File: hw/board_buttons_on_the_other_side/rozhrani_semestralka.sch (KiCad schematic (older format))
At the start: 59 parts, among them P1 DISPLAY_CONN, P2 DISPLAY_VCC_CON, P3 USB_B, Q1 BC847, U1 MCP2210, U2 MIC5504-3.3, U3 Joystick, U4 LM239, U5 CD4532, U6 NPIC6C596, U7 NE555, U8 PB6149L, U9 PB6149Ldual

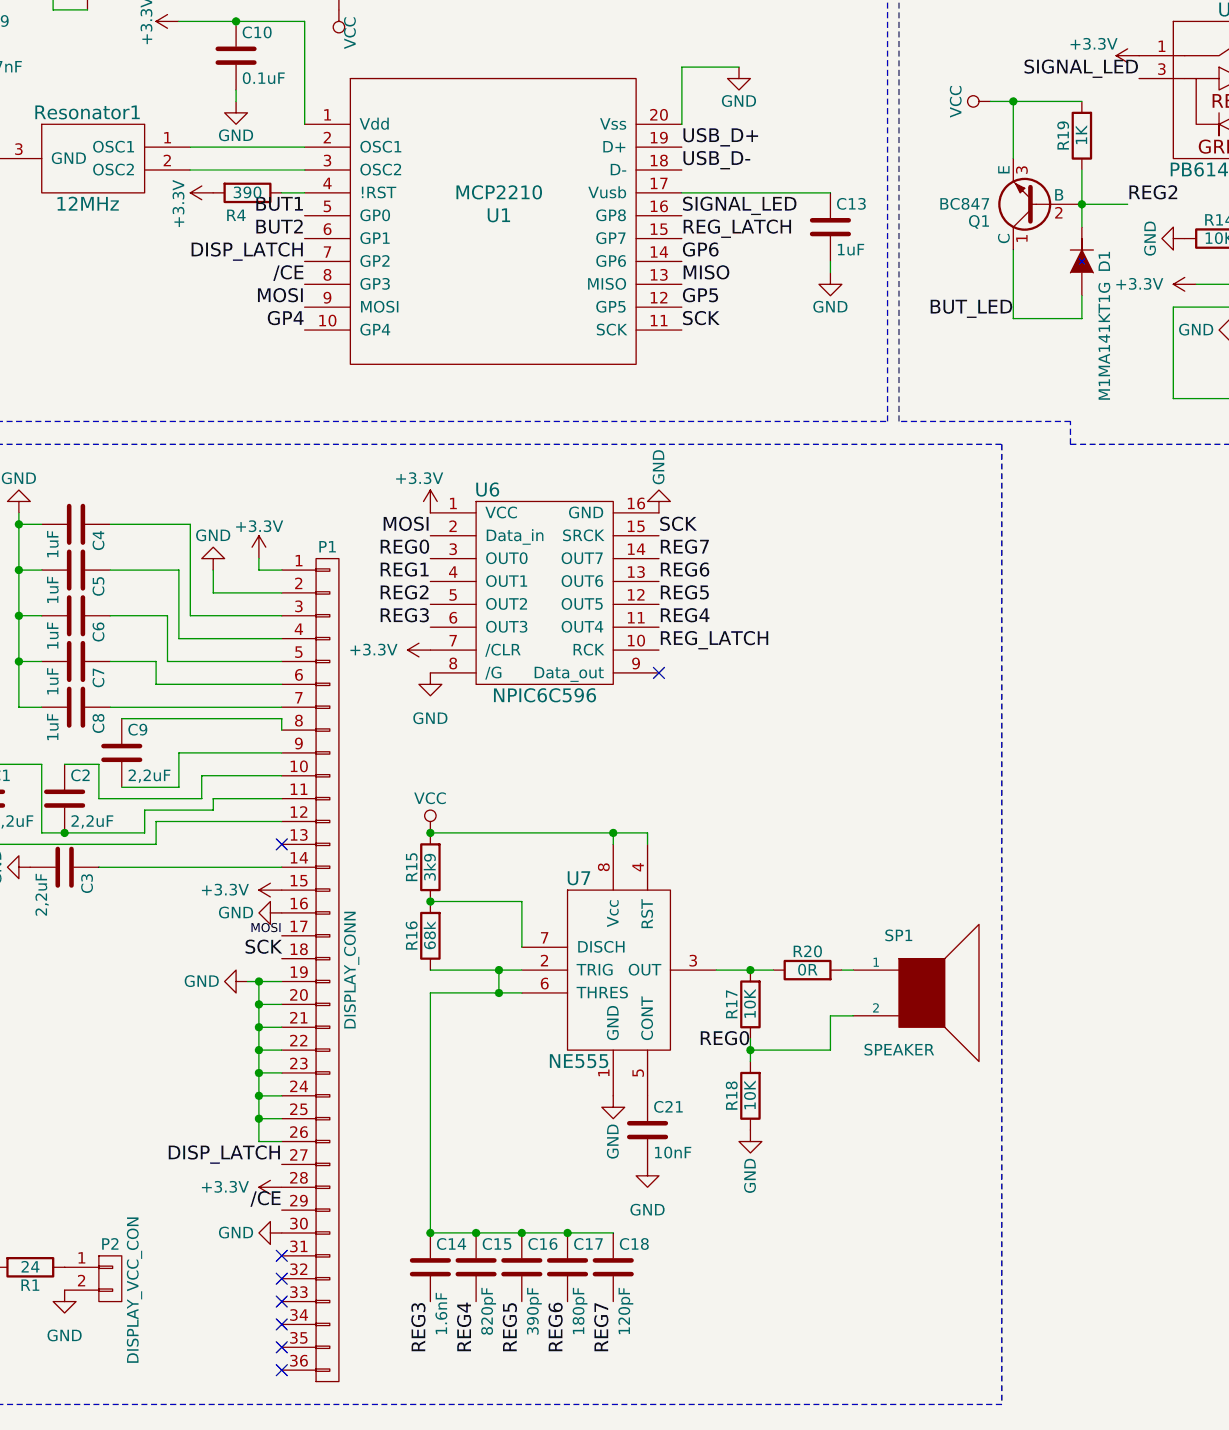
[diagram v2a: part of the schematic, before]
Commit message: Aladin v 1.2.0 pcb - repaired GPIO for /CE and also BUZZERs capacitors, some footprints had change
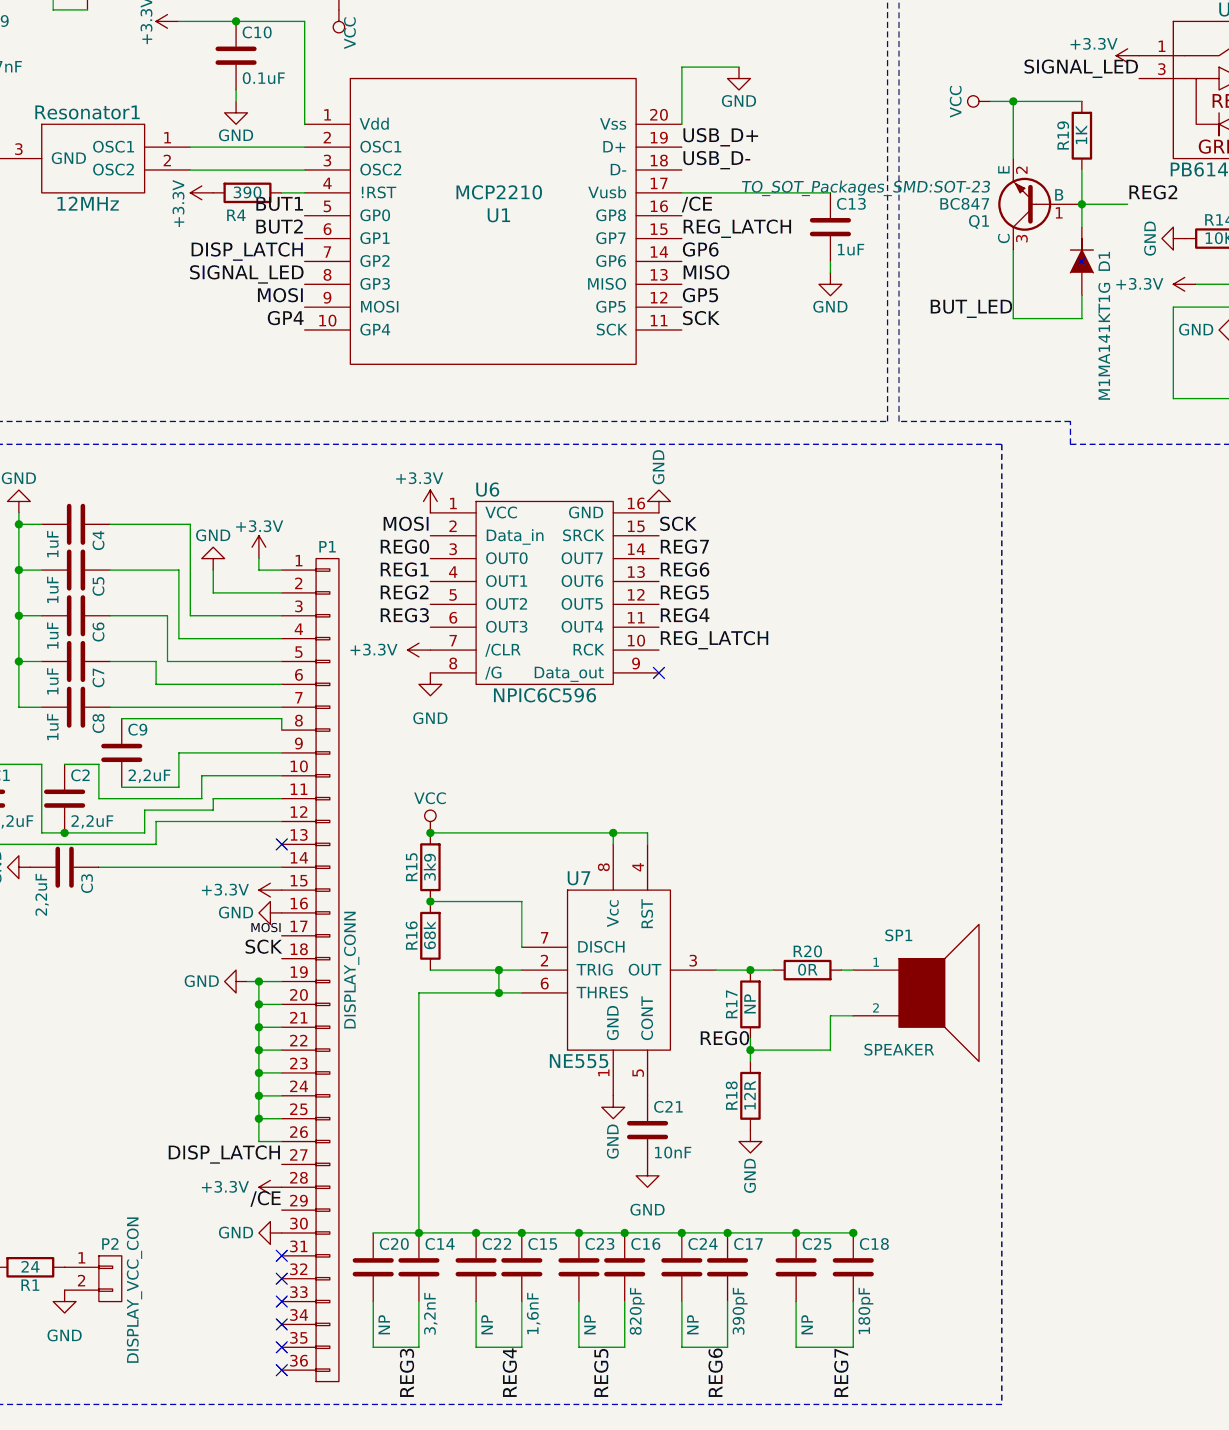
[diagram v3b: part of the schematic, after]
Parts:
- removed Q1: BC847, TO_SOT_Packages_SMD:SOT-323, symbol BC547
- added C20, C22, C23, C24, C25: NP, Capacitors_SMD:C_0603_HandSoldering, symbol C
- added Q1: BC847, TO_SOT_Packages_SMD:SOT-23, symbol BC849
- C14: value 1.6nF -> 3,2nF
- C15: value 820pF -> 1,6nF
- C16: value 390pF -> 820pF
- C17: value 180pF -> 390pF
- C18: value 120pF -> 180pF
- R17: value 10K -> NP
- R18: value 10K -> 12R
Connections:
- net /CE: now also U1.16 (GP8); no longer U1.8 (GP3)
- net BUT_LED: now also Q1.3 (C)
- net REG2: now also Q1.1 (B)
- net REG3: now also C20.2
- net REG4: now also C22.2
- net REG5: now also C23.2
- net REG6: now also C24.2
- net REG7: now also C25.2
- net SIGNAL_LED: now also U1.8 (GP3); no longer U1.16 (GP8)
- net VCC: now also Q1.2 (E)
- net at C14.1, C15.1, C16.1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: now also C20.1, C22.1, C23.1, C24.1, C25.1
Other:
- moved on the sheet: C14, C15, C16, C17, C18
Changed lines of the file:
@@
 Text Label 10200 2250 0    60   ~ 0
 JOY_DOWN
-Text Label 2500 2750 2    60   ~ 0
+Text Label 4150 2450 0    60   ~ 0
 /CE
 Text Label 2500 2650 2    60   ~ 0
@@
 P 4450 5900
 F 0 "R17" V 4530 5900 50  0000 C CNN
-F 1 "10K" V 4450 5900 50  0000 C CNN
+F 1 "NP" V 4450 5900 50  0000 C CNN
 F 2 "Resistors_SMD:R_0603_HandSoldering" V 4380 5900 30  0001 C CNN
 F 3 "" H 4450 5900 30  0000 C CNN
@@
 P 4450 6300
 F 0 "R18" V 4530 6300 50  0000 C CNN
-F 1 "10K" V 4450 6300 50  0000 C CNN
+F 1 "12R" V 4450 6300 50  0000 C CNN
 F 2 "Resistors_SMD:R_0603_HandSoldering" V 4380 6300 30  0001 C CNN
 F 3 "" H 4450 6300 30  0000 C CNN
@@
 L C C15
 U 1 1 56ED13E4
-P 3250 7050
-F 0 "C15" H 3275 7150 50  0000 L CNN
-F 1 "820pF" V 3300 6750 50  0000 L CNN
-F 2 "Capacitors_SMD:C_0603_HandSoldering" H 3288 6900 30  0001 C CNN
-F 3 "" H 3250 7050 60  0000 C CNN
-	1    3250 7050
-	1    0    0    -1
-$EndComp
-$Comp
-L C C16
-U 1 1 56ED1814
 P 3450 7050
-F 0 "C16" H 3475 7150 50  0000 L CNN
-F 1 "390pF" V 3500 6750 50  0000 L CNN
+F 0 "C15" H 3475 7150 50  0000 L CNN
+F 1 "1,6nF" V 3500 6750 50  0000 L CNN
 F 2 "Capacitors_SMD:C_0603_HandSoldering" H 3488 6900 30  0001 C CNN
 F 3 "" H 3450 7050 60  0000 C CNN
@@
 $EndComp
 $Comp
+L C C16
+U 1 1 56ED1814
+P 3900 7050
+F 0 "C16" H 3925 7150 50  0000 L CNN
+F 1 "820pF" V 3950 6750 50  0000 L CNN
+F 2 "Capacitors_SMD:C_0603_HandSoldering" H 3938 6900 30  0001 C CNN
+F 3 "" H 3900 7050 60  0000 C CNN
+	1    3900 7050
+	1    0    0    -1
+$EndComp
+$Comp
 L C C17
 U 1 1 56ED18B7
-P 3650 7050
-F 0 "C17" H 3675 7150 50  0000 L CNN
-F 1 "180pF" V 3700 6750 50  0000 L CNN
-F 2 "Capacitors_SMD:C_0603_HandSoldering" H 3688 6900 30  0001 C CNN
-F 3 "" H 3650 7050 60  0000 C CNN
-	1    3650 7050
+P 4350 7050
+F 0 "C17" H 4375 7150 50  0000 L CNN
+F 1 "390pF" V 4400 6750 50  0000 L CNN
+F 2 "Capacitors_SMD:C_0603_HandSoldering" H 4388 6900 30  0001 C CNN
+F 3 "" H 4350 7050 60  0000 C CNN
+	1    4350 7050
 	1    0    0    -1
 $EndComp
@@
 L C C18
 U 1 1 56ED195B
-P 3850 7050
-F 0 "C18" H 3875 7150 50  0000 L CNN
-F 1 "120pF" V 3900 6750 50  0000 L CNN
-F 2 "Capacitors_SMD:C_0603_HandSoldering" H 3888 6900 30  0001 C CNN
-F 3 "" H 3850 7050 60  0000 C CNN
-	1    3850 7050
+P 4900 7050
+F 0 "C18" H 4925 7150 50  0000 L CNN
+F 1 "180pF" V 4950 6750 50  0000 L CNN
+F 2 "Capacitors_SMD:C_0603_HandSoldering" H 4938 6900 30  0001 C CNN
+F 3 "" H 4900 7050 60  0000 C CNN
+	1    4900 7050
 	1    0    0    -1
 $EndComp
@@
 L C C14
 U 1 1 56ED1C02
-P 3050 7050
-F 0 "C14" H 3075 7150 50  0000 L CNN
-F 1 "1.6nF" V 3100 6750 50  0000 L CNN
-F 2 "Capacitors_SMD:C_0603_HandSoldering" H 3088 6900 30  0001 C CNN
-F 3 "" H 3050 7050 60  0000 C CNN
-	1    3050 7050
+P 3000 7050
+F 0 "C14" H 3025 7150 50  0000 L CNN
+F 1 "3,2nF" V 3050 6750 50  0000 L CNN
+F 2 "Capacitors_SMD:C_0603_HandSoldering" H 3038 6900 30  0001 C CNN
+F 3 "" H 3000 7050 60  0000 C CNN
+	1    3000 7050
 	1    0    0    -1
 $EndComp
@@
 Text Label 3050 4250 2    60   ~ 0
 REG3
-Text Label 3050 7200 3    60   ~ 0
+Text Label 3000 7400 3    60   ~ 0
 REG3
 Text Label 4050 4250 0    60   ~ 0
@@
 Text Label 4050 4150 0    60   ~ 0
 REG5
-Text Label 3250 7200 3    60   ~ 0
+Text Label 3450 7400 3    60   ~ 0
 REG4
-Text Label 3450 7200 3    60   ~ 0
+Text Label 3850 7400 3    60   ~ 0
 REG5
 Text Label 4050 4050 0    60   ~ 0
 REG6
-Text Label 3650 7200 3    60   ~ 0
+Text Label 4350 7400 3    60   ~ 0
 REG6
 Text Label 4050 3950 0    60   ~ 0
 REG7
-Text Label 3850 7200 3    60   ~ 0
+Text Label 4900 7400 3    60   ~ 0
 REG7
 Text Label 3050 3950 2    60   ~ 0
@@
 Text Label 8800 1400 3    60   ~ 0
 JOY_DOWN
-Text Label 4150 2450 0    60   ~ 0
+Text Label 2500 2750 2    60   ~ 0
 SIGNAL_LED
 $Comp
@@
 $EndComp
 $Comp
-L BC547 Q1
-U 1 1 5803C382
-P 5700 2400
-F 0 "Q1" H 5900 2475 50  0000 L CNN
-F 1 "BC847" H 5900 2400 50  0000 L CNN
-F 2 "TO_SOT_Packages_SMD:SOT-323" H 5900 2325 50  0001 L CIN
-F 3 "" H 5700 2400 50  0000 L CNN
-	1    5700 2400
-	-1   0    0    1
-$EndComp
-$Comp
 L R R19
 U 1 1 5803E27E
@@
 Wire Wire Line
 	4450 6050 4450 6150
-Connection ~ 3250 6900
 Connection ~ 3450 6900
-Connection ~ 3650 6900
 Connection ~ 3350 5850
 Connection ~ 4450 5750
@@
 	650  3450 5550 3450
 Wire Wire Line
-	3050 5850 3050 6900
-Wire Wire Line
-	3450 5850 3050 5850
-Connection ~ 3050 6900
+	3000 5850 3450 5850
+Connection ~ 3000 6900
 Wire Wire Line
 	3050 5150 4000 5150
@@
 Connection ~ 6150 900
 Wire Wire Line
-	3050 6900 3850 6900
+	2800 6900 4900 6900
 Wire Wire Line
 	6950 1300 6950 1400
@@
 NoConn ~ 4050 4450
 NoConn ~ 2400 7500
+$Comp
+L C C20
+U 1 1 58735AB0
+P 2800 7050
+F 0 "C20" H 2825 7150 50  0000 L CNN
+F 1 "NP" V 2850 6750 50  0000 L CNN
+F 2 "Capacitors_SMD:C_0603_HandSoldering" H 2838 6900 30  0001 C CNN
+F 3 "" H 2800 7050 60  0000 C CNN
+	1    2800 7050
+	1    0    0    -1
+$EndComp
+$Comp
+L C C22
+U 1 1 58735B7A
+P 3250 7050
+F 0 "C22" H 3275 7150 50  0000 L CNN
+F 1 "NP" V 3300 6750 50  0000 L CNN
+F 2 "Capacitors_SMD:C_0603_HandSoldering" H 3288 6900 30  0001 C CNN
+F 3 "" H 3250 7050 60  0000 C CNN
+	1    3250 7050
+	1    0    0    -1
+$EndComp
+$Comp
+L C C23
+U 1 1 58735C41
+P 3700 7050
+F 0 "C23" H 3725 7150 50  0000 L CNN
+F 1 "NP" V 3750 6750 50  0000 L CNN
+F 2 "Capacitors_SMD:C_0603_HandSoldering" H 3738 6900 30  0001 C CNN
+F 3 "" H 3700 7050 60  0000 C CNN
+	1    3700 7050
+	1    0    0    -1
+$EndComp
+$Comp
+L C C24
+U 1 1 58735D0F
+P 4150 7050
+F 0 "C24" H 4175 7150 50  0000 L CNN
+F 1 "NP" V 4200 6750 50  0000 L CNN
+F 2 "Capacitors_SMD:C_0603_HandSoldering" H 4188 6900 30  0001 C CNN
+F 3 "" H 4150 7050 60  0000 C CNN
+	1    4150 7050
+	1    0    0    -1
+$EndComp
+$Comp
+L C C25
+U 1 1 58735DE0
+P 4650 7050
+F 0 "C25" H 4675 7150 50  0000 L CNN
+F 1 "NP" V 4700 6750 50  0000 L CNN
+F 2 "Capacitors_SMD:C_0603_HandSoldering" H 4688 6900 30  0001 C CNN
+F 3 "" H 4650 7050 60  0000 C CNN
+	1    4650 7050
+	1    0    0    -1
+$EndComp
+Wire Wire Line
+	3000 6900 3000 5850
+Connection ~ 3250 6900
+Connection ~ 3700 6900
+Connection ~ 3900 6900
+Connection ~ 4150 6900
+Connection ~ 4350 6900
+Connection ~ 4650 6900
+Connection ~ 4900 6900
+Wire Wire Line
+	3000 7200 3000 7400
+Wire Wire Line
+	2800 7200 2800 7400
+Wire Wire Line
+	2800 7400 3000 7400
+Wire Wire Line
+	3250 7200 3250 7400
+Wire Wire Line
+	3250 7400 3450 7400
+Wire Wire Line
+	3450 7400 3450 7200
+Wire Wire Line
+	3700 7200 3700 7400
+Wire Wire Line
+	3700 7400 3900 7400
+Wire Wire Line
+	3900 7400 3900 7200
+Wire Wire Line
+	4150 7200 4150 7400
+Wire Wire Line
+	4150 7400 4350 7400
+Wire Wire Line
+	4350 7400 4350 7200
+Wire Wire Line
+	4650 7200 4650 7400
+Wire Wire Line
+	4650 7400 4900 7400
+Wire Wire Line
+	4900 7400 4900 7200
+$Comp
+L BC849 Q1
+U 1 1 587757B2
+P 5700 2400
+F 0 "Q1" H 5900 2475 50  0000 L CNN
+F 1 "BC847" H 5900 2400 50  0000 L CNN
+F 2 "TO_SOT_Packages_SMD:SOT-23" H 5900 2325 50  0000 L CIN
+F 3 "" H 5700 2400 50  0000 L CNN
+	1    5700 2400
+	-1   0    0    1
+$EndComp
 $EndSCHEMATC
